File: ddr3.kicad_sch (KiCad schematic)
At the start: 61 parts

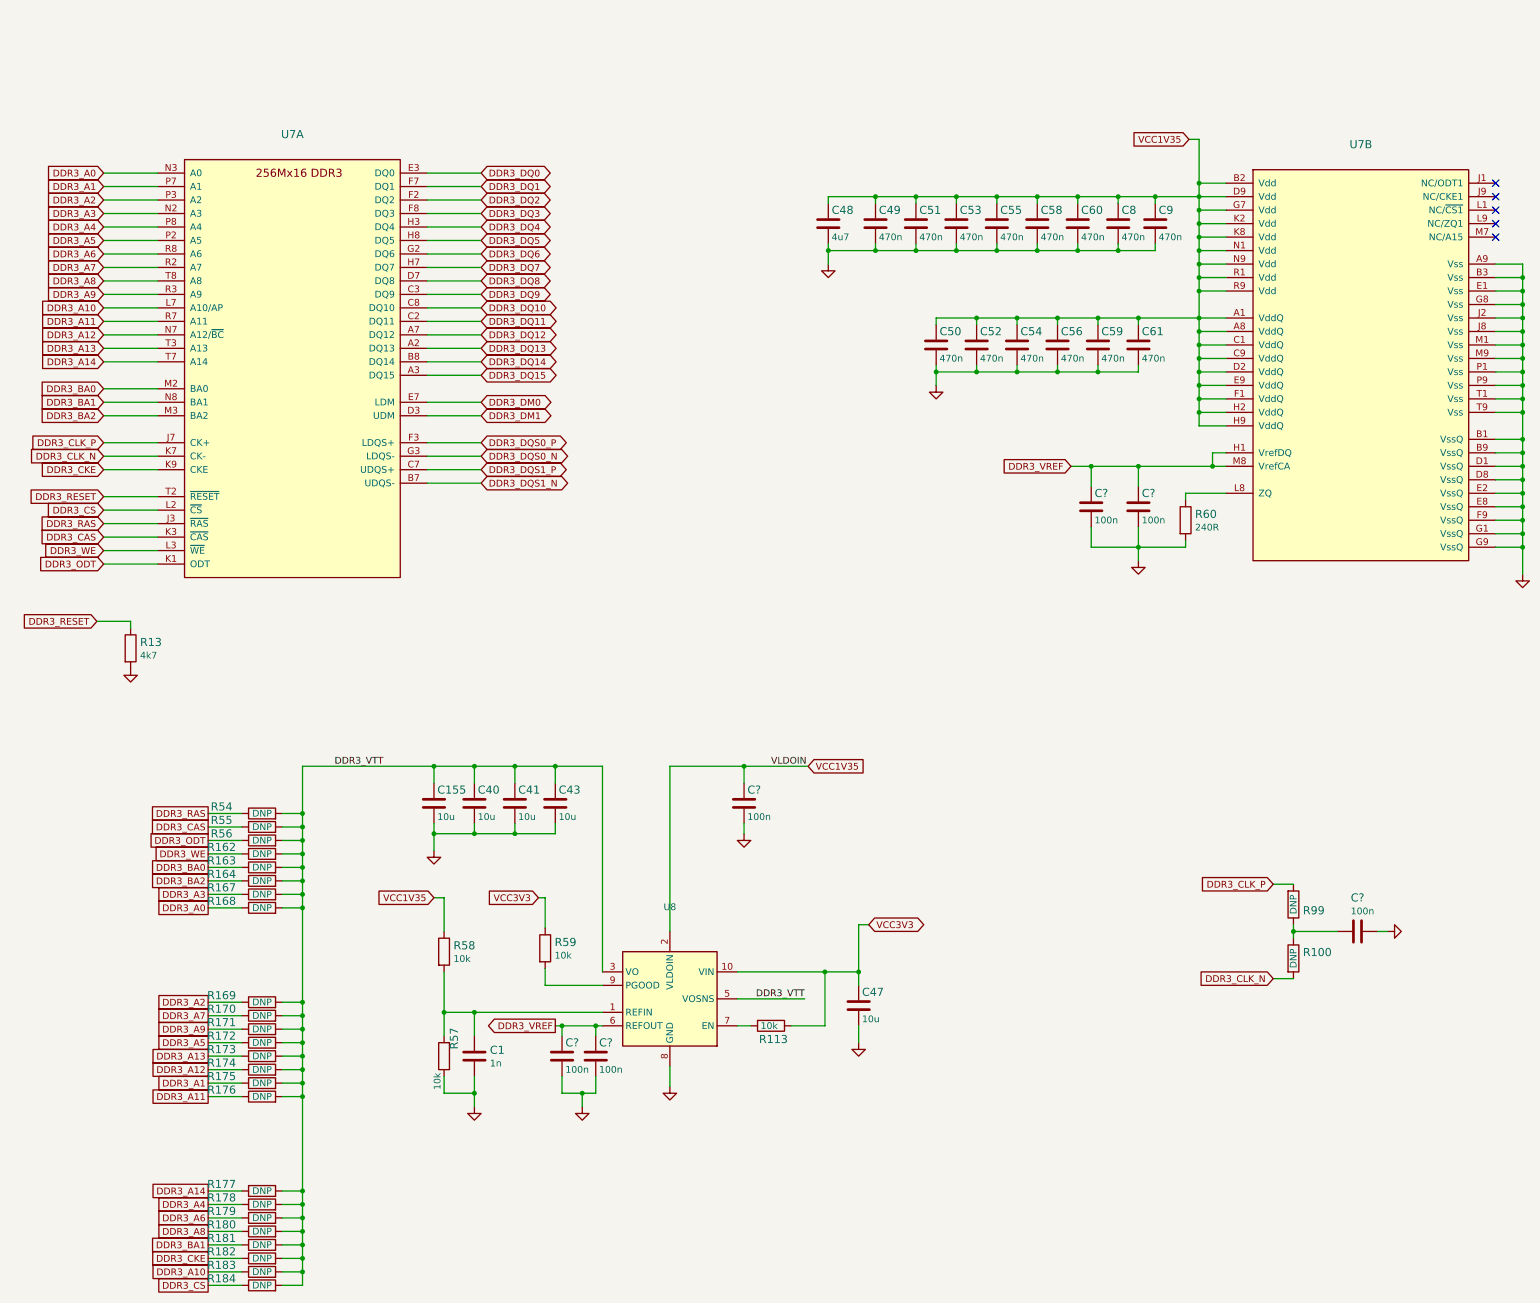
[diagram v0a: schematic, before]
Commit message: Introduce component standardization
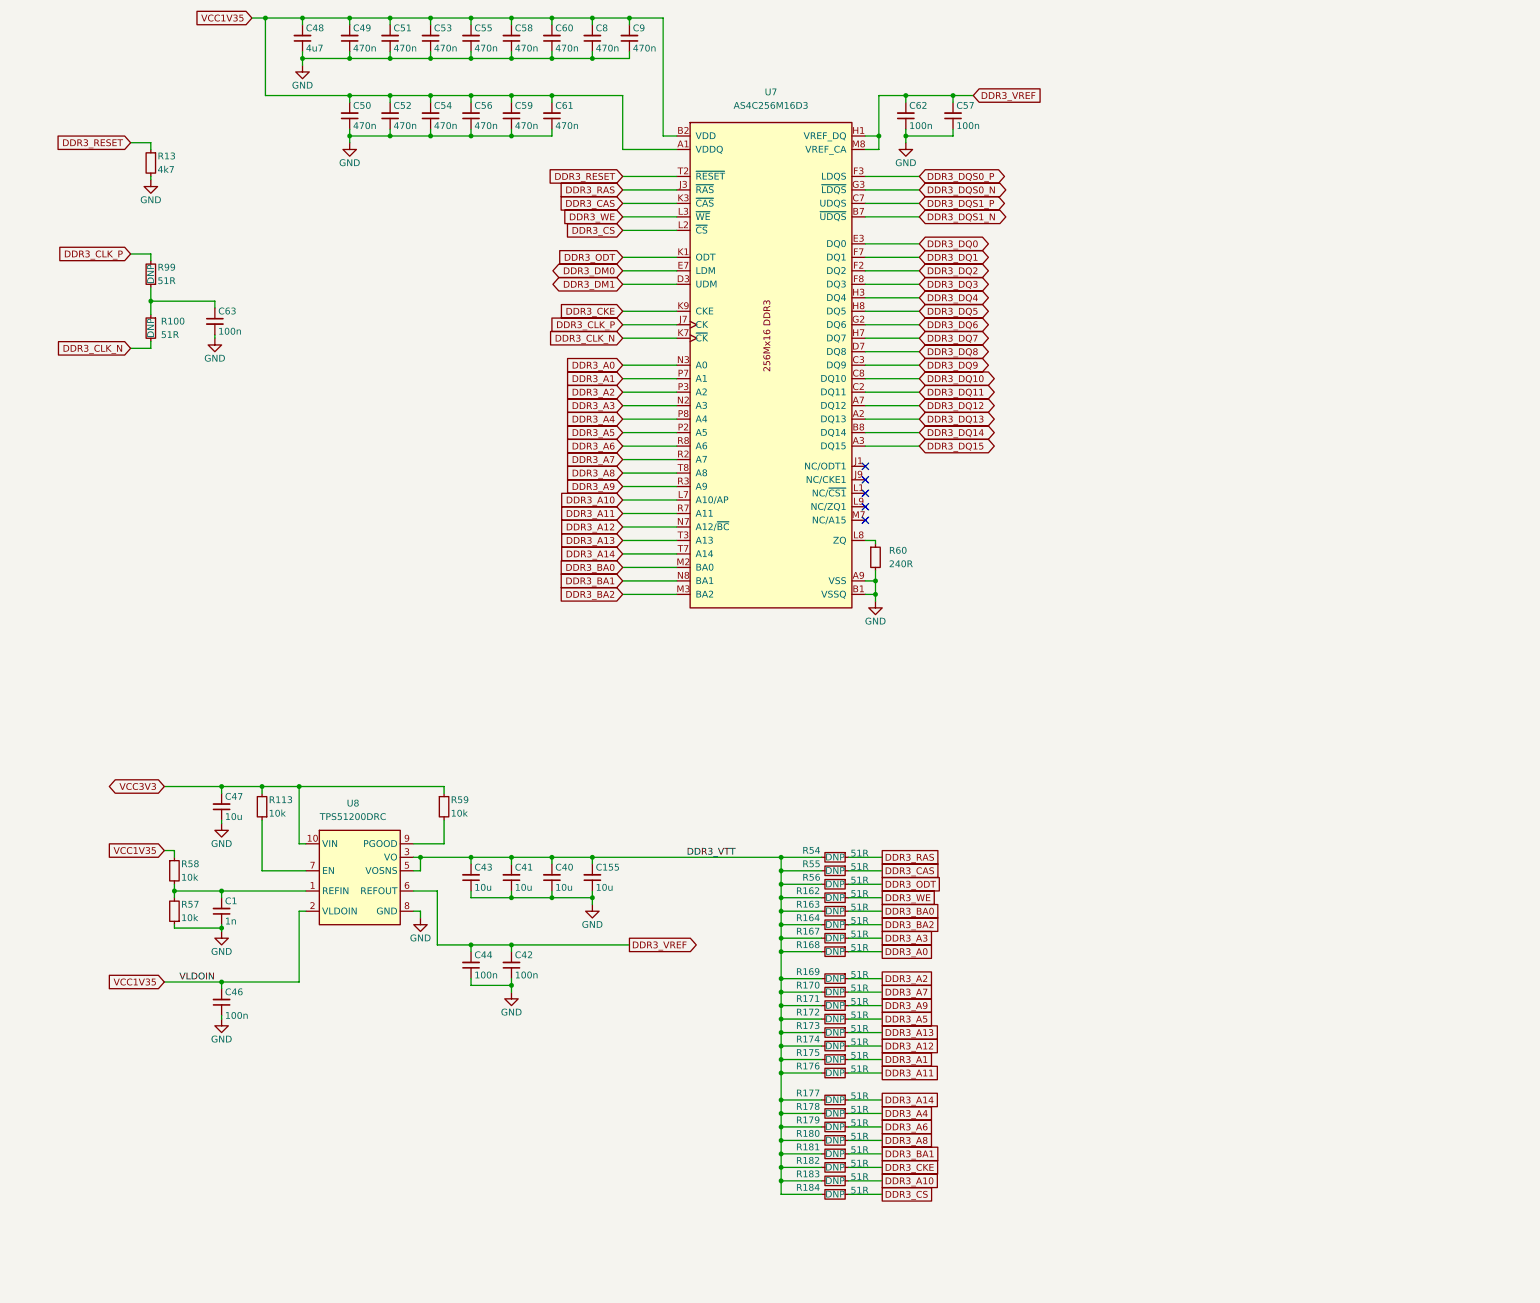
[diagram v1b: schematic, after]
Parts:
- removed unit 2 of U7
- C1: value (none) -> C_1n_0402; footprint (none) -> antmicro-footprints:C_0402_1005Metric; symbol artix-dc-scm:C_1n_0402 -> antmicroCapacitors0402:C_1n_0402; Author (none) -> Antmicro; Dielectric (none) -> C0G; License (none) -> Apache-2.0; MPN CC0402KRX7R9BB102 -> GRM1555C1H102JA01D; Manufacturer YAGEO -> Murata; Voltage (none) -> 50V
- C155, C40, C41, C43, C47: value (none) -> C_10u_0402; footprint (none) -> antmicro-footprints:C_0402_1005Metric; symbol artix-dc-scm:C_10u_0402 -> antmicroCapacitors0402:C_10u_0402; Author (none) -> Antmicro; License (none) -> Apache-2.0; MPN GRM155R60J106ME44D -> CC0402MRX5R5BB106; Manufacturer MURATA -> Yaego
- C42, C44, C46, C57, C62, C63: renamed from C?; value (none) -> C_100n_6V3_0402; footprint (none) -> antmicro-footprints:C_0402_1005Metric; symbol artix-dc-scm:C_100n_0402-artix-dc-scm -> antmicroCapacitorsmisc:C_100n_6V3_0402; Author (none) -> Antmicro; License (none) -> Apache-2.0
- C48: value (none) -> C_4u7_0402; footprint (none) -> antmicro-footprints:C_0402_1005Metric; symbol artix-dc-scm:C_4u7_0402 -> antmicroCapacitors0402:C_4u7_0402; Author (none) -> Antmicro; License (none) -> Apache-2.0; Manufacturer MURATA -> Murata
- C49, C50, C51, C52, C53, C54, C55, C56, C58, C59, C60, C61, C8, C9: value (none) -> C_470n_0402; footprint (none) -> antmicro-footprints:C_0402_1005Metric; symbol artix-dc-scm:C_470n_0402 -> antmicroCapacitors0402:C_470n_0402; Author (none) -> Antmicro; License (none) -> Apache-2.0
- R100, R162, R163, R164, R167, R168, R169, R170, R171, R172, R173, R174, R175, R176, R177, R178, R179, R180, R181, R182, R183, R184, R54, R55, R56, R99: value (none) -> R_51R_0402; footprint (none) -> antmicro-footprints:R_0402_1005Metric; symbol artix-dc-scm:R_51R_0402 -> antmicroResistors0402:R_51R_0402; Author (none) -> Antmicro; License (none) -> Apache-2.0; MPN RC0402FR-0751RL -> CR0402-FX-51R0GLF; Manufacturer YAGEO -> Bourns; Tolerance (none) -> 1%
- R113, R57, R58, R59: value (none) -> R_10k_0402; footprint (none) -> antmicro-footprints:R_0402_1005Metric; symbol artix-dc-scm:R_10k_0402 -> antmicroResistors0402:R_10k_0402; Author (none) -> Antmicro; License (none) -> Apache-2.0; MPN CRCW040210K0FKEDHP -> CR0402-FX-1002GLF; Manufacturer VISHAY -> Bourns; Tolerance (none) -> 1%
- R13: value (none) -> R_4k7_0402; footprint (none) -> antmicro-footprints:R_0402_1005Metric; symbol artix-dc-scm:R_4k7_0402 -> antmicroResistors0402:R_4k7_0402; Author (none) -> Antmicro; License (none) -> Apache-2.0; MPN ERJ2GEJ472X -> CR0402-FX-4701GLF; Manufacturer PANASONIC_ELECTRONIC_COMPONENTS -> Bourns; Tolerance (none) -> 1%
- R60: value (none) -> R_240R_0402; footprint (none) -> antmicro-footprints:R_0402_1005Metric; symbol artix-dc-scm:R_240R_0402 -> antmicroResistors0402:R_240R_0402; Author (none) -> Antmicro; License (none) -> Apache-2.0; MPN ERJ2GEJ241X -> CR0402-FX-2400GLF; Manufacturer PANASONIC -> Bourns; Tolerance (none) -> 1%
- U7: value (none) -> AS4C256M16D3; footprint (none) -> antmicro-footprints:BGA-96_9.0x13.0mm_Layout2x3x16_P0.8mm; symbol artix-dc-scm:AS4C256M16D3 -> antmicroMemory:AS4C256M16D3; Author (none) -> Antmicro; License (none) -> Apache-2.0; MPN (none) -> AS4C256M16D3; Manufacturer (none) -> Alliance Memory
- U8: value (none) -> TPS51200DRC; footprint (none) -> antmicro-footprints:VSON-10-1EP_3x3mm; symbol artix-dc-scm:TPS51200DRC -> antmicroPMICVoltageRegulatorsDCDCSwitchingControllers:TPS51200DRC; Author (none) -> Antmicro; License (none) -> Apache-2.0; MPN (none) -> TPS51200DRC; Manufacturer (none) -> Texas Instruments
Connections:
- net DDR3_VREF: now also C42.2, C44.2, C57.2, C62.2, U7.H1 (VREF_DQ), U7.M8 (VREF_CA); no longer C42.1, C44.1, C57.1, C62.1
- net DDR3_VTT: now also C155.2, C40.2, C41.2, C43.2; no longer C155.1, C40.1, C41.1, C43.1
- net GND: now also C1.1, C155.1, C40.1, C41.1, C42.1, C43.1, C44.1, C46.1, C47.1, C48.1, C49.1, C50.1, C51.1, C52.1, C53.1, C54.1, C55.1, C56.1, C57.1, C58.1, C59.1, C60.1, C61.1, C62.1, C63.2, C8.1, C9.1, U7.A9 (VSS), U7.B1 (VSSQ), U7.B3 (VSS), U7.B9 (VSSQ), U7.D1 (VSSQ), U7.D8 (VSSQ), U7.E1 (VSS), U7.E2 (VSSQ), U7.E8 (VSSQ), U7.F9 (VSSQ), U7.G1 (VSSQ), U7.G8 (VSS), U7.G9 (VSSQ), U7.J2 (VSS), U7.J8 (VSS), U7.M1 (VSS), U7.M9 (VSS), U7.P1 (VSS), U7.P9 (VSS), U7.T1 (VSS), U7.T9 (VSS); no longer C1.2, C155.2, C40.2, C41.2, C42.2, C43.2, C44.2, C46.2, C47.2, C48.2, C49.2, C50.2, C51.2, C52.2, C53.2, C54.2, C55.2, C56.2, C57.2, C58.2, C59.2, C60.2, C61.2, C62.2, C63.1, C8.2, C9.2
- net VCC1V35: now also C46.2, C48.2, C49.2, C50.2, C51.2, C52.2, C53.2, C54.2, C55.2, C56.2, C58.2, C59.2, C60.2, C61.2, C8.2, C9.2, U7.A1 (VDDQ), U7.A8 (VDDQ), U7.B2 (VDD), U7.C1 (VDDQ), U7.C9 (VDDQ), U7.D2 (VDDQ), U7.D9 (VDD), U7.E9 (VDDQ), U7.F1 (VDDQ), U7.G7 (VDD), U7.H2 (VDDQ), U7.H9 (VDDQ), U7.K2 (VDD), U7.K8 (VDD), U7.N1 (VDD), U7.N9 (VDD), U7.R1 (VDD), U7.R9 (VDD); no longer C46.1, C48.1, C49.1, C50.1, C51.1, C52.1, C53.1, C54.1, C55.1, C56.1, C58.1, C59.1, C60.1, C61.1, C8.1, C9.1
- net VCC3V3: now also C47.2, R113.2; no longer C47.1, R113.1
- net at R100.1, R99.1: now also C63.1; no longer C63.2
- net at U8.7 (EN): now also R113.1; no longer R113.2
- net at R57.2, R58.2, U8.1 (REFIN): now also C1.2; no longer C1.1
- net at R60.1: now also U7.L8 (ZQ)
- new net: U7.J1 (NC/ODT1), U7.J9 (NC/CKE1), U7.L1 (NC/~{CS1}), U7.L9 (NC/ZQ1), U7.M7 (NC/A15), U7.T7
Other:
- moved on the sheet: C1, C155, C40, C41, C42, C43, C44, C46, C47, C48, C49, C50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

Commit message: Bump revision to 1.1.1
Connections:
- net at U7.J1 (NC/ODT1): now also U7.J9 (NC/CKE1), U7.L1 (NC/~{CS1}), U7.L9 (NC/ZQ1), U7.M7 (NC/A15), U7.T7
- now unconnected: U7.J9 (NC/CKE1), U7.L1 (NC/~{CS1}), U7.L9 (NC/ZQ1), U7.M7 (NC/A15)
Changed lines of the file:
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@@
   (title_block
     (title "Artix - Datacenter Secure Control Module (DC-SCM)")
-    (date "2023-06-06")
-    (rev "1.1.0")
+    (date "2023-08-09")
+    (rev "1.1.1")
   )
   (junction (at 161.925 52.07) (diameter 0) (color 0 0 0 0)

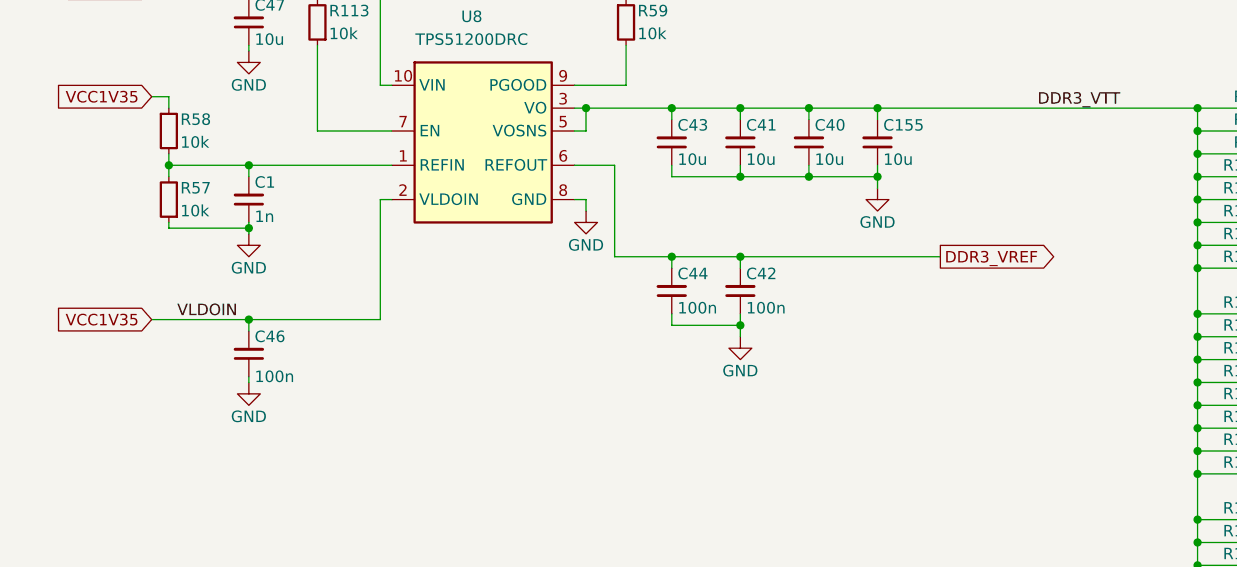
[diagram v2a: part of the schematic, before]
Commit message: Fix schematic ERC errors. ERC clean
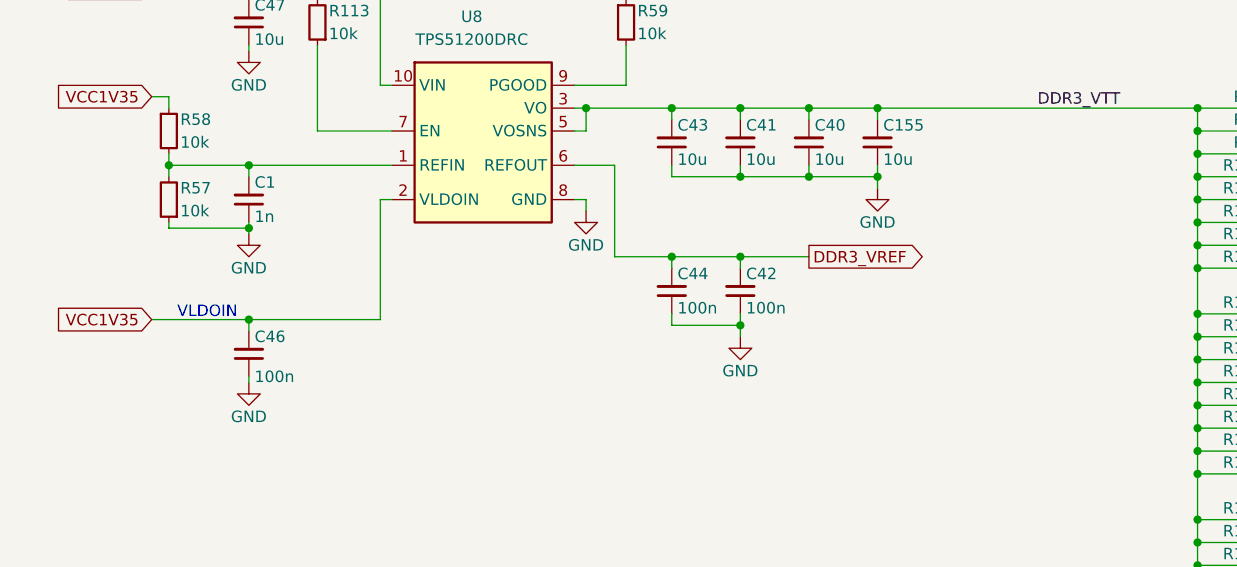
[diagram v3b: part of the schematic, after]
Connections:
- now unconnected: U7.J1 (NC/ODT1), U7.J9 (NC/CKE1), U7.L1 (NC/~{CS1}), U7.L9 (NC/ZQ1), U7.M7 (NC/A15)
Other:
- note added: "VLDOIN"
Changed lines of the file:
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@@
     (stroke (width 0) (type default) (color 0 0 0 0))
   )
+  (wire (pts (xy 169.545 212.09) (xy 177.165 212.09))
+    (stroke (width 0) (type default) (color 0 0 0 0))
+  )
   (wire (pts (xy 177.165 37.465) (xy 184.785 37.465))
     (stroke (width 0) (type default) (color 0 0 0 0))
@@
     (stroke (width 0) (type default) (color 0 0 0 0))
   )
-  (wire (pts (xy 169.545 212.09) (xy 191.77 212.09))
-    (stroke (width 0) (type default) (color 0 0 0 0))
-  )
   (wire (pts (xy 161.925 203.2) (xy 169.545 203.2))
     (stroke (width 0) (type default) (color 0 0 0 0))
@@
     (stroke (width 0) (type default) (color 0 0 0 0))
   )
-  (label "VLDOIN" (at 113.665 219.075 180)
+  (text "VLDOIN" (at 113.665 219.075 180)
     (effects (font (size 1.27 1.27)) (justify right bottom))
   )
@@
     )
   )
-  (global_label "DDR3_VREF" (shape output) (at 191.77 212.09 0) (fields_autoplaced)
+  (global_label "DDR3_VREF" (shape output) (at 177.165 212.09 0) (fields_autoplaced)
     (effects (font (size 1.27 1.27)) (justify left))
-    (property "Intersheet References" "${INTERSHEET_REFS}" (id 0) (at 369.57 -15.24 0)
+    (property "Intersheet References" "${INTERSHEET_REFS}" (id 0) (at 354.965 -15.24 0)
       (effects (font (size 1.27 1.27)) (justify left) hide)
     )
@@
       (effects (font (size 1.27 1.27)) hide)
     )
+    (property "Author" "Antmicro" (id 4) (at 110.49 75.565 0)
+      (effects (font (size 1.27 1.27) (thickness 0.15)) (justify left bottom) hide)
+    )
+    (property "License" "Apache-2.0" (id 5) (at 110.49 78.105 0)
+      (effects (font (size 1.27 1.27) (thickness 0.15)) (justify left bottom) hide)
+    )
     (pin "1")
   )
@@
       (effects (font (size 1.27 1.27)) hide)
     )
+    (property "Author" "Antmicro" (id 4) (at 123.825 217.17 0)
+      (effects (font (size 1.27 1.27) (thickness 0.15)) (justify left bottom) hide)
+    )
+    (property "License" "Apache-2.0" (id 5) (at 123.825 219.71 0)
+      (effects (font (size 1.27 1.27) (thickness 0.15)) (justify left bottom) hide)
+    )
     (pin "1")
   )
@@
       (effects (font (size 1.27 1.27)) hide)
     )
+    (property "Author" "Antmicro" (id 4) (at 160.655 228.6 0)
+      (effects (font (size 1.27 1.27) (thickness 0.15)) (justify left bottom) hide)
+    )
+    (property "License" "Apache-2.0" (id 5) (at 160.655 231.14 0)
+      (effects (font (size 1.27 1.27) (thickness 0.15)) (justify left bottom) hide)
+    )
     (pin "1")
   )
@@
       (effects (font (size 1.27 1.27)) hide)
     )
+    (property "Author" "Antmicro" (id 4) (at 175.895 212.09 0)
+      (effects (font (size 1.27 1.27) (thickness 0.15)) (justify left bottom) hide)
+    )
+    (property "License" "Apache-2.0" (id 5) (at 175.895 214.63 0)
+      (effects (font (size 1.27 1.27) (thickness 0.15)) (justify left bottom) hide)
+    )
     (pin "1")
   )
@@
       (effects (font (size 1.27 1.27)) hide)
     )
+    (property "Author" "Antmicro" (id 4) (at 106.045 233.68 0)
+      (effects (font (size 1.27 1.27) (thickness 0.15)) (justify left bottom) hide)
+    )
+    (property "License" "Apache-2.0" (id 5) (at 106.045 236.22 0)
+      (effects (font (size 1.27 1.27) (thickness 0.15)) (justify left bottom) hide)
+    )
     (pin "1")
   )
@@
       (effects (font (size 1.27 1.27)) hide)
     )
+    (property "Author" "Antmicro" (id 4) (at 143.51 214.63 0)
+      (effects (font (size 1.27 1.27) (thickness 0.15)) (justify left bottom) hide)
+    )
+    (property "License" "Apache-2.0" (id 5) (at 143.51 217.17 0)
+      (effects (font (size 1.27 1.27) (thickness 0.15)) (justify left bottom) hide)
+    )
     (pin "1")
   )
@@
       (effects (font (size 1.27 1.27)) hide)
     )
+    (property "Author" "Antmicro" (id 4) (at 106.045 196.85 0)
+      (effects (font (size 1.27 1.27) (thickness 0.15)) (justify left bottom) hide)
+    )
+    (property "License" "Apache-2.0" (id 5) (at 106.045 199.39 0)
+      (effects (font (size 1.27 1.27) (thickness 0.15)) (justify left bottom) hide)
+    )
     (pin "1")
   )
@@
       (effects (font (size 1.27 1.27)) hide)
     )
+    (property "Author" "Antmicro" (id 4) (at 139.065 53.975 0)
+      (effects (font (size 1.27 1.27) (thickness 0.15)) (justify left bottom) hide)
+    )
+    (property "License" "Apache-2.0" (id 5) (at 139.065 56.515 0)
+      (effects (font (size 1.27 1.27) (thickness 0.15)) (justify left bottom) hide)
+    )
     (pin "1")
   )
@@
       (effects (font (size 1.27 1.27)) hide)
     )
+    (property "Author" "Antmicro" (id 4) (at 147.955 68.58 0)
+      (effects (font (size 1.27 1.27) (thickness 0.15)) (justify left bottom) hide)
+    )
+    (property "License" "Apache-2.0" (id 5) (at 147.955 71.12 0)
+      (effects (font (size 1.27 1.27) (thickness 0.15)) (justify left bottom) hide)
+    )
     (pin "1")
   )
@@
       (effects (font (size 1.27 1.27)) hide)
     )
+    (property "Author" "Antmicro" (id 4) (at 234.95 68.58 0)
+      (effects (font (size 1.27 1.27) (thickness 0.15)) (justify left bottom) hide)
+    )
+    (property "License" "Apache-2.0" (id 5) (at 234.95 71.12 0)
+      (effects (font (size 1.27 1.27) (thickness 0.15)) (justify left bottom) hide)
+    )
     (pin "1")
   )
@@
       (effects (font (size 1.27 1.27)) hide)
     )
+    (property "Author" "Antmicro" (id 4) (at 122.555 105.41 0)
+      (effects (font (size 1.27 1.27) (thickness 0.15)) (justify left bottom) hide)
+    )
+    (property "License" "Apache-2.0" (id 5) (at 122.555 107.95 0)
+      (effects (font (size 1.27 1.27) (thickness 0.15)) (justify left bottom) hide)
+    )
     (pin "1")
   )
@@
       (effects (font (size 1.27 1.27)) hide)
     )
+    (property "Author" "Antmicro" (id 4) (at 247.015 154.94 0)
+      (effects (font (size 1.27 1.27) (thickness 0.15)) (justify left bottom) hide)
+    )
+    (property "License" "Apache-2.0" (id 5) (at 247.015 157.48 0)
+      (effects (font (size 1.27 1.27) (thickness 0.15)) (justify left bottom) hide)
+    )
     (pin "1")
